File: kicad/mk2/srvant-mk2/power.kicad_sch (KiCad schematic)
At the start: 70 parts, among them J1 Barrel_Jack_Switch, J12 Screw_Terminal_01x02, J2 Conn_01x02, Q1 DMP3013SFV-7, U1 AP63205WU, U15 TLV62585DRLR, U2 AP64501SP-13, U3 74AHC1G32, U4 INA219AxDCN, U9 RT9742SNGV

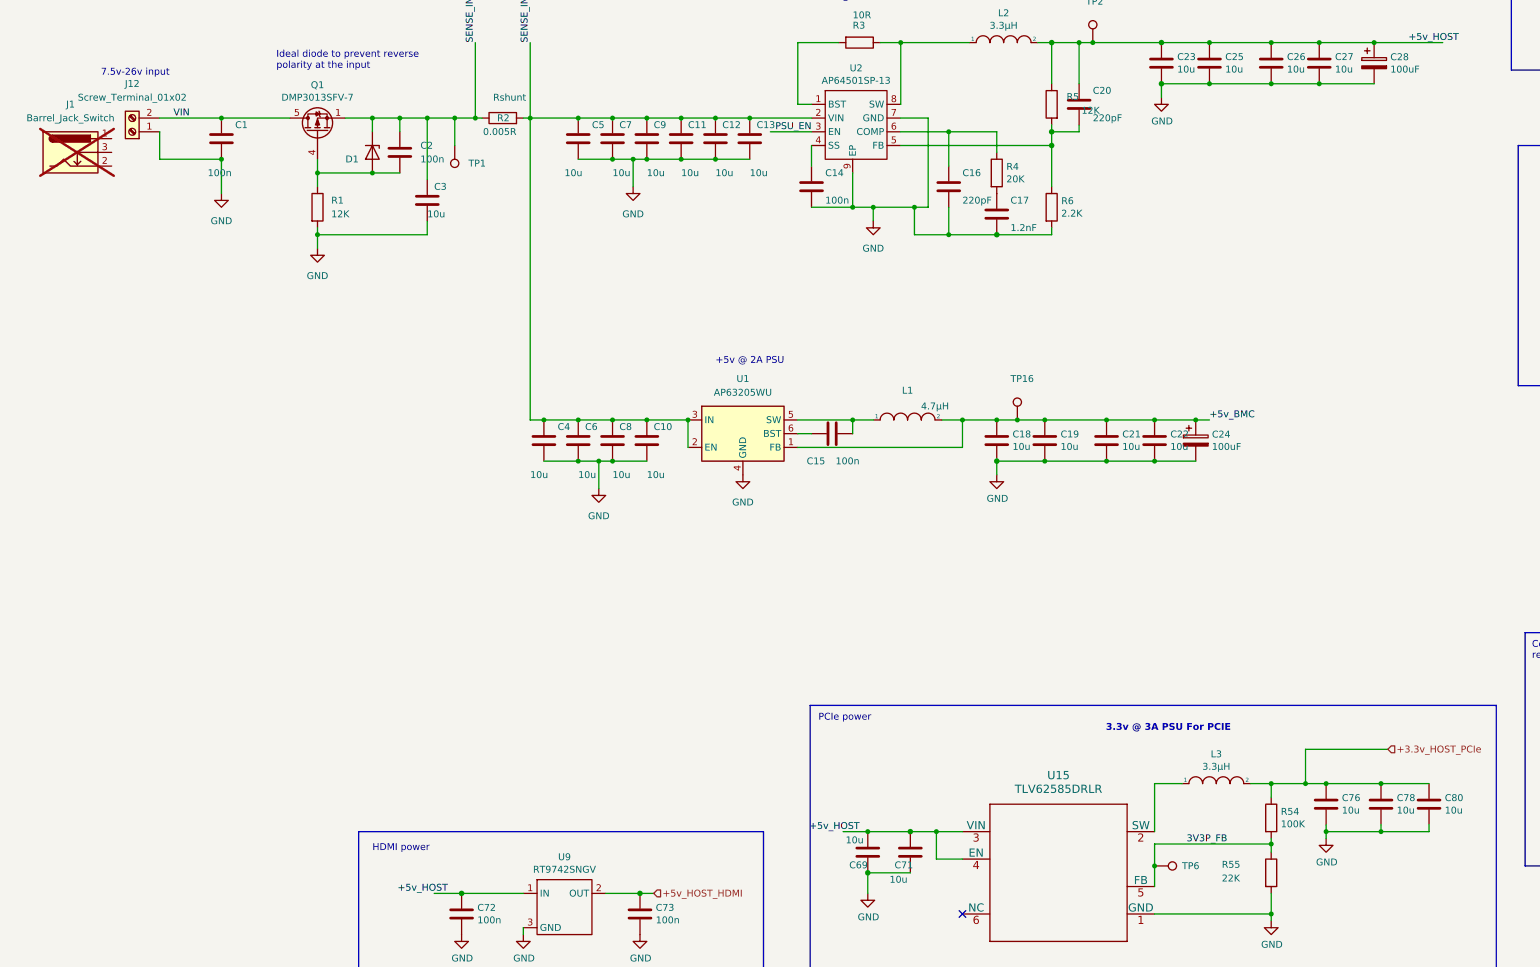
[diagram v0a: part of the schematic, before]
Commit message: reroute diff pairs
Reroute all diff pairs after another run with the jlcpcb calculator.
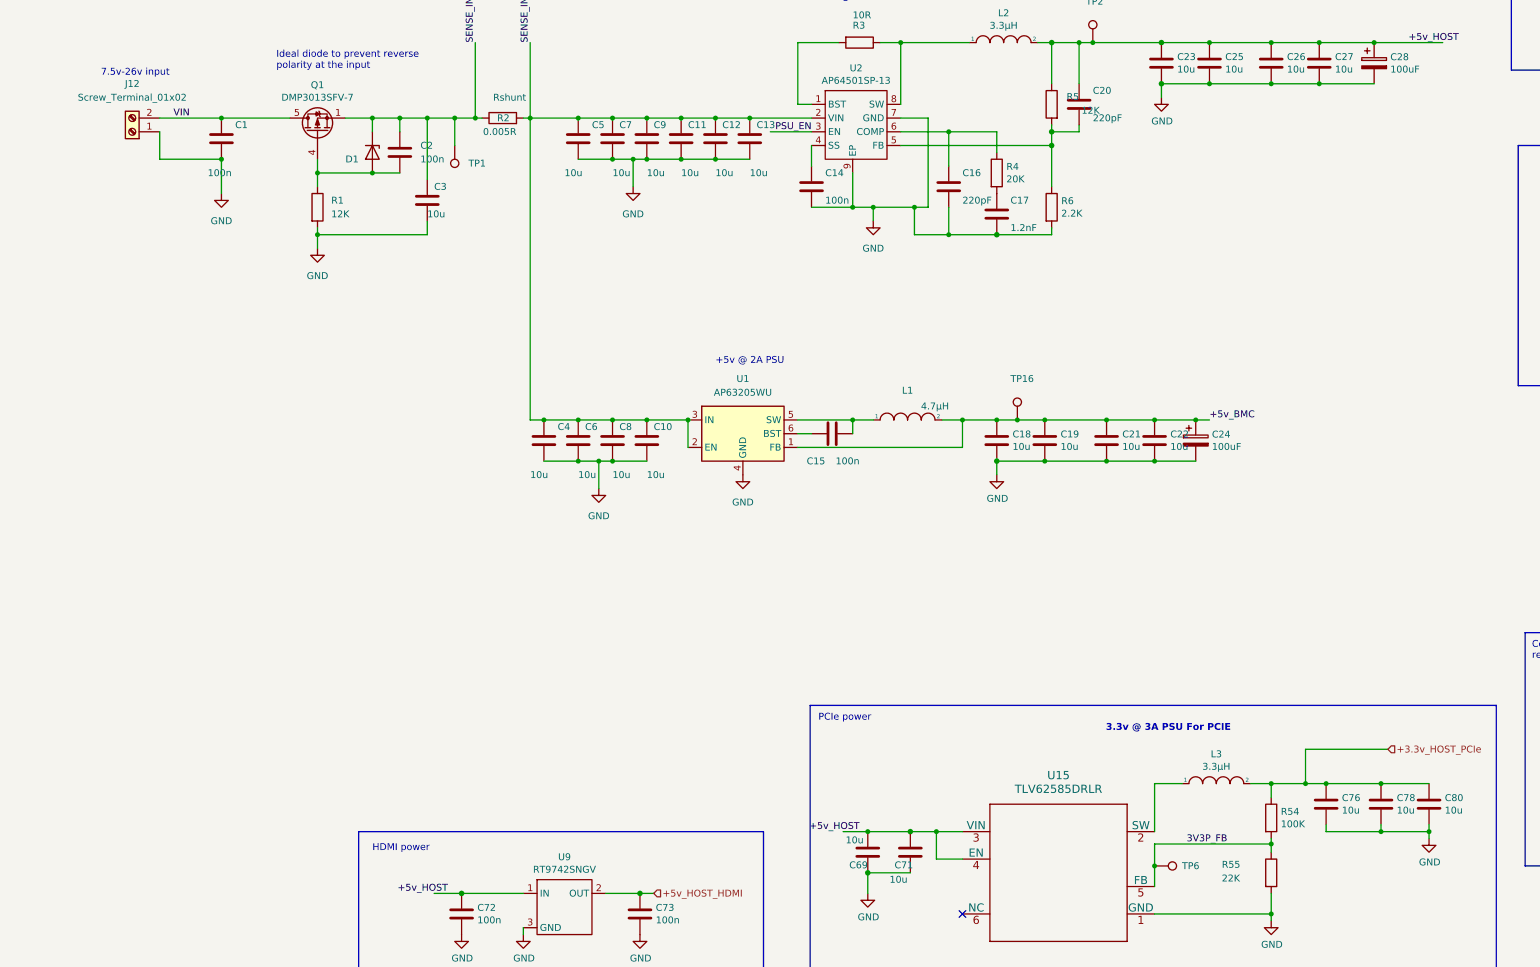
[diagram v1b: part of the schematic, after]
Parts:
- removed J1: Barrel_Jack_Switch, Connector_BarrelJack:BarrelJack_Horizontal, symbol ARJM11:Barrel_Jack_Switch
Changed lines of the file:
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@@
   (junction (at 273.05 243.84) (diameter 0) (color 0 0 0 0)
   )
-  (junction (at 262.89 243.84) (diameter 0) (color 0 0 0 0)
-  )
   (junction (at 261.62 97.79) (diameter 0) (color 0 0 0 0)
   )
@@
   (junction (at 175.26 167.64) (diameter 0) (color 0 0 0 0)
   )
+  (junction (at 281.94 243.84) (diameter 0) (color 0 0 0 0)
+  )
   (junction (at 222.25 175.26) (diameter 0) (color 0 0 0 0)
   )
@@
     (stroke (width 0) (type default))
   )
-  (wire (pts (xy 262.89 245.11) (xy 262.89 243.84))
+  (wire (pts (xy 281.94 245.11) (xy 281.94 243.84))
     (stroke (width 0) (type default))
   )
@@
     )
   )
-  (symbol (lib_id "ARJM11:Barrel_Jack_Switch") (at 30.48 118.11 0) (unit 1)
-    (in_bom no) (on_board no) (dnp yes) (fields_autoplaced)
-    (property "Reference" "J1" (at 30.48 109.22 0)
-      (effects (font (size 1.27 1.27)))
-    )
-    (property "Value" "Barrel_Jack_Switch" (at 30.48 111.76 0)
-      (effects (font (size 1.27 1.27)))
-    )
-    (property "Footprint" "Connector_BarrelJack:BarrelJack_Horizontal" (at 31.75 119.126 0)
-      (effects (font (size 1.27 1.27)) hide)
-    )
-    (property "Datasheet" "https://www.we-online.com/catalog/datasheet/694106301002.pdf" (at 31.75 119.126 0)
-      (effects (font (size 1.27 1.27)) hide)
-    )
-    (property "manf#" "694106301002" (at 30.48 118.11 0)
-      (effects (font (size 1.27 1.27)) hide)
-    )
-    (property "digikey#" "" (at 30.48 118.11 0)
-      (effects (font (size 1.27 1.27)) hide)
-    )
-    (property "mouser#" "710-694106301002" (at 30.48 118.11 0)
-      (effects (font (size 1.27 1.27)) hide)
-    )
-    (property "farnell#" "" (at 30.48 118.11 0)
-      (effects (font (size 1.27 1.27)) hide)
-    )
-    (property "rs#" "" (at 30.48 118.11 0)
-      (effects (font (size 1.27 1.27)) hide)
-    )
-    (property "Part Description" "" (at 30.48 118.11 0)
-      (effects (font (size 1.27 1.27)) hide)
-    )
-    (property "Sim.Enable" "0" (at 30.48 118.11 0)
-      (effects (font (size 1.27 1.27)) hide)
-    )
-    (pin "1")
-    (pin "2")
-    (pin "3")
-    (instances
-      (project "srvant-mk2"
-        (path "/1859a578-b791-4142-bdf4-fda494df1146/c300a602-5caa-44c4-bd60-e0bac469451e"
-          (reference "J1") (unit 1)
-        )
-      )
-    )
-  )
   (symbol (lib_id "Device:C") (at 232.41 101.6 0) (unit 1)
     (in_bom yes) (on_board yes) (dnp no)
@@
     )
   )
-  (symbol (lib_id "power:GND") (at 262.89 245.11 0) (unit 1)
+  (symbol (lib_id "power:GND") (at 281.94 245.11 0) (unit 1)
     (in_bom yes) (on_board yes) (dnp no)
-    (property "Reference" "#PWR051" (at 262.89 251.46 0)
+    (property "Reference" "#PWR051" (at 281.94 251.46 0)
       (effects (font (size 1.27 1.27)) hide)
     )
-    (property "Value" "GND" (at 263.017 249.5042 0)
+    (property "Value" "GND" (at 282.067 249.5042 0)
       (effects (font (size 1.27 1.27)))
     )
-    (property "Footprint" "" (at 262.89 245.11 0)
+    (property "Footprint" "" (at 281.94 245.11 0)
       (effects (font (size 1.27 1.27)) hide)
     )
-    (property "Datasheet" "" (at 262.89 245.11 0)
+    (property "Datasheet" "" (at 281.94 245.11 0)
       (effects (font (size 1.27 1.27)) hide)
     )

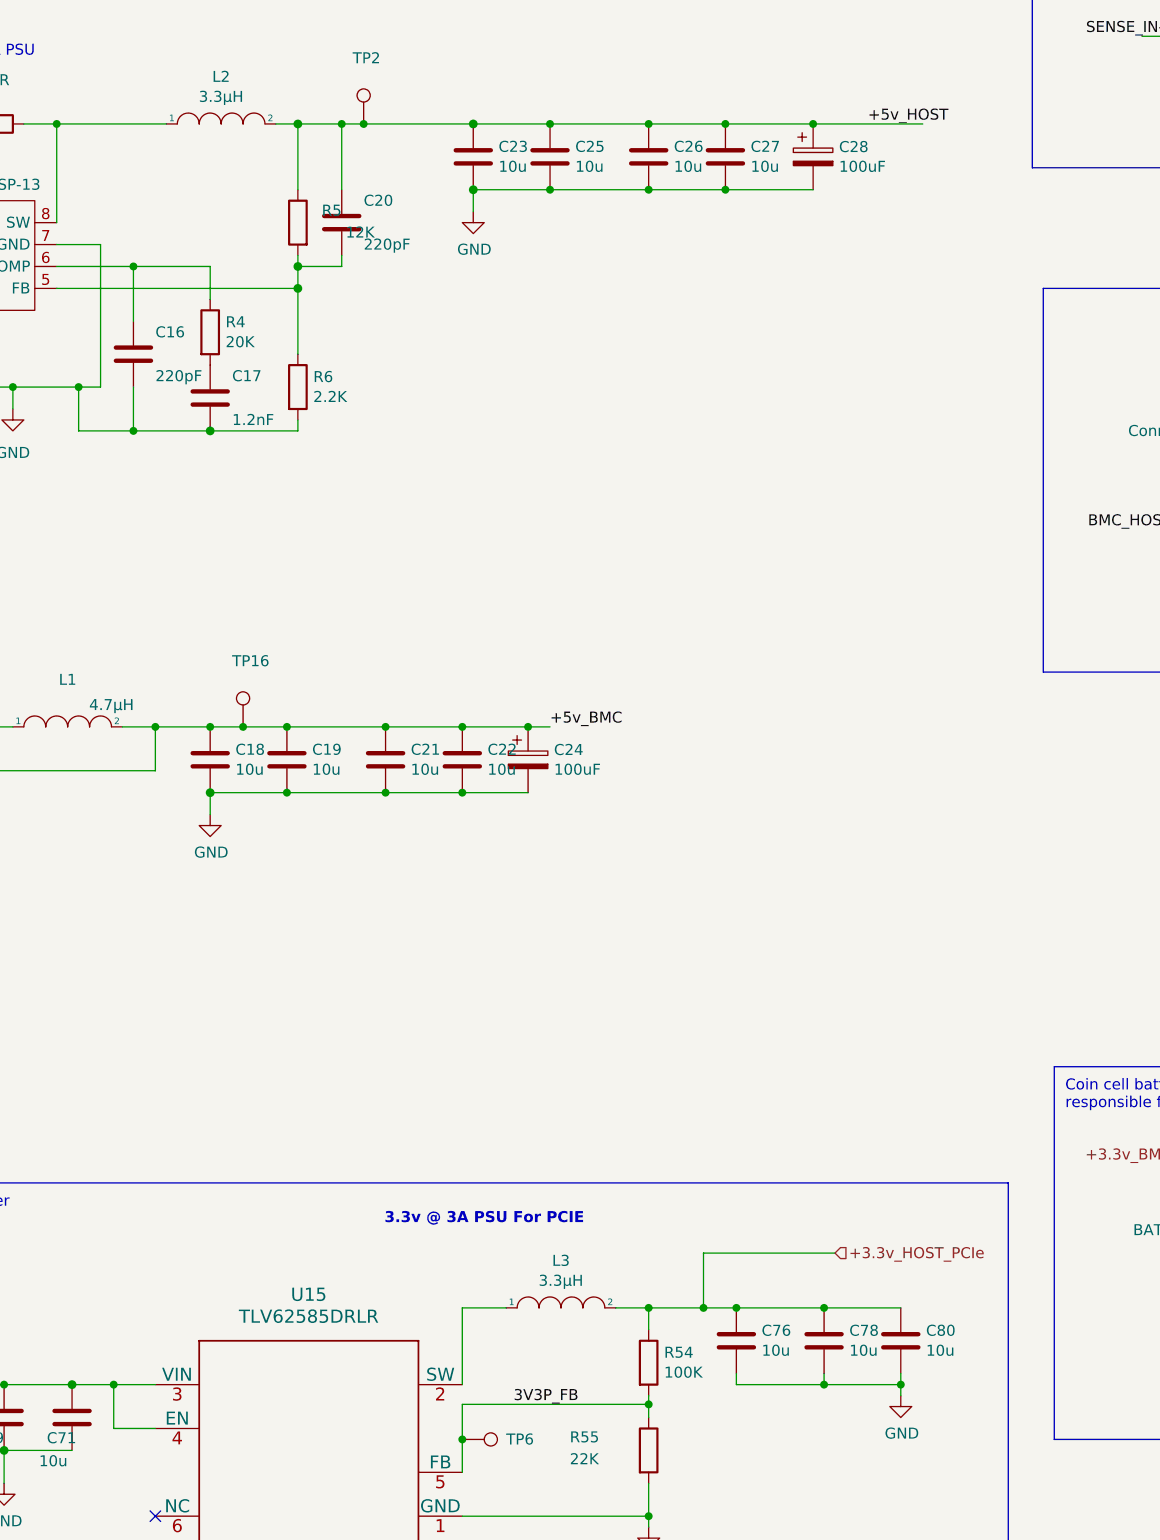
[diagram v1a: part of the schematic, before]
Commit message: lot's of small updates
* fix the quartz footprint
* fix wrong inductor in pcie power unit
* fix lots of descriptions,uids
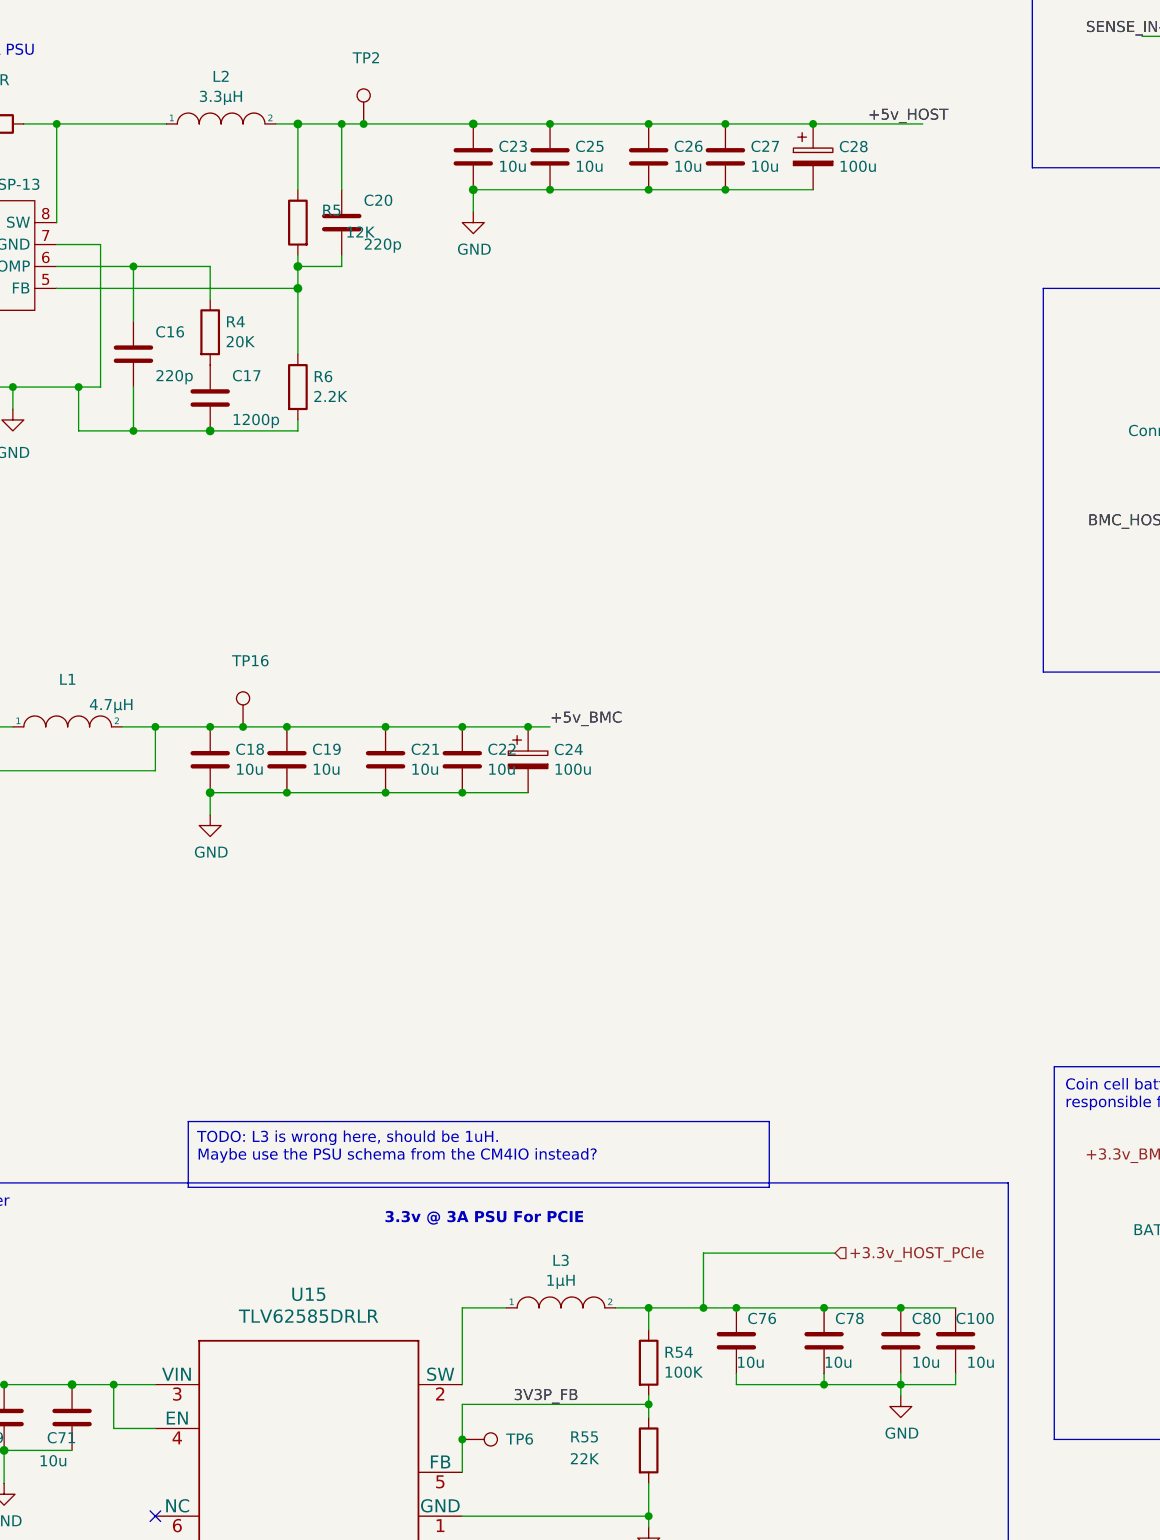
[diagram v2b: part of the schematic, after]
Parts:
- added C100: 10u, Capacitor_SMD:C_0805_2012Metric, symbol Device:C
- C16, C20: value 220pF -> 220p
- C17: value 1.2nF -> 1200p
- C18, C19, C21, C22, C23, C25, C26, C27: Field5 (none) -> 490-10505-1-ND; Field6 (none) -> GRM21BC8YA106KE11L; Field7 (none) -> Murata
- C24, C28: value 100uF -> 100u; mouser# 667-EEF-CX0J101R -> ECASD40J107M015K00
- C69, C71: Field8 (none) -> 111893011
- C76, C78, C80: Field5 490-14381-1-ND -> 490-10505-1-ND; Field6 GRM21BR71A106KA73L -> GRM21BC8YA106KE11L
- L1: farnell# (none) -> 2329227
- L3: value 3.3µH -> 1µH; Field4 Farnell -> (none); Field5 2616889 -> (none); Field6 SRN6045TA-3R3Y -> (none); Field7 Bourns -> (none); Part Description 3.3µH Semi-Shielded Wirewound Inductor 7.8A 21mOhm Nonstand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 -> 1µH Semi-Shielded Wirewound Inductor 8A; farnell# (none) -> 2616885; manf# (none) -> SRN6045TA-1R0Y
- R1: Part Description (none) -> Resistor 12K M1005 1% 63mW; farnell# (none) -> 9239367; manf# (none) -> MCR01MZPF1202
- R55: farnell# (none) -> 9239430; manf# (none) -> RC0402FR-0747KL
- R7, R8: Part Description (none) -> Resistor 10R M1005 1% 63mW
- U3: farnell# (none) -> 3120315
- U4: farnell# (none) -> 3118164
- U9: manf# (none) -> RT9742SNGV; mouser# (none) -> 835-RT9742SNGV
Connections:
- net +3.3v_HOST_PCIe: now also C100.1
- net GND: now also C100.2
